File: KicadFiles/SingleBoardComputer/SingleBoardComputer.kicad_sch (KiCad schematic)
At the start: 12 parts

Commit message: Schematic v1.0 done
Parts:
- added C1, C10, C13, C15, C16, C17, C18, C19, C20, C3, C4, C5, C6, C9: 10uF, symbol Device:C
- added C11, C12, C2: 100nF, symbol Device:C
- added C14: 4.7uF, symbol Device:C
- added C7, C8: 47pF, symbol Device:C
- added D1, D2, D3, D4, D5, D6: LED, symbol Device:LED
- added FB1: FerriteBead, symbol Device:FerriteBead
- added L1: 2.2uH, symbol Device:L
- added R1, R10, R11, R2, R5, R6, R7, R8, R9: 5.1k, symbol Device:R
- added R12, R13, R14, R15, R16, R17: 220, symbol Device:R
- added R3, R4: 27, symbol Device:R
- added TP1, TP2, TP3, TP4, TP5, TP6, TP7, TP8, TP? (x2): TestPoint, symbol Connector:TestPoint
- added U3: ISL9110IRT7Z-T7A, Package_DFN_QFN:DFN-12-1EP_3x3mm_P0.5mm_EP1.6x2.5mm_ThermalVias, symbol CustomComponents:ISL9110IRT7Z-T7A
- J1: renamed from J?; symbol Connector:USB_C_Receptacle_USB2.0_16P -> CustomComponents:USB_C_Receptacle_USB2.0_16P_Custom
- SW1: renamed from SW?; footprint (none) -> Button_Switch_SMD:SW_SPST_PTS647_Sx38
- U4, U6: renamed from U?; symbol Memory_Flash:SST39SF040 -> CustomComponents:SST39SF040_Custom
- gave numbers to parts that had none: 8
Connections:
- net USBTP3V3 is gone; now on net UTP_3V3: U5.15 (3V3OUT), U5.3 (VCCIO)
- net +3V3: now also U1.2 (VO), C16.1, C17.1, C18.1, C5.1, D3.2 (A), R10.1, R11.1
- net +5V: now also U1.3 (VI), U4.31 (~{WE}), U6.31 (~{WE}), U8.12 (BGACK), U8.13 (BR), U8.23 (VPA), U8.24 (BERR), C1.1, C10.1, C13.1, C15.1, C19.1, C2.1, C20.1, C3.1, C4.1, D1.2 (A), R5.1, R6.1, R7.1, R8.1, R9.1, U3.1 (VOUT), U3.12 (FB); no longer U5.18 (VCC)
- net A10: now also U2.26 (A9), U4.26 (A9), U6.26 (A9); no longer U2.27 (A8), U4.27 (A8), U6.27 (A8)
- net A11: now also U2.25 (A10), U4.23 (A10), U6.23 (A10); no longer U2.26 (A9), U4.26 (A9), U6.26 (A9)
- net A12: now also U2.24 (A11), U4.25 (A11), U6.25 (A11); no longer U2.25 (A10), U4.23 (A10), U6.23 (A10)
- net A13: now also U2.21 (A12), U4.4 (A12), U6.4 (A12); no longer U2.24 (A11), U4.25 (A11), U6.25 (A11)
- net A14: now also U2.20 (A13), U4.28 (A13), U6.28 (A13); no longer U2.21 (A12), U4.4 (A12), U6.4 (A12)
- net A15: now also U2.19 (A14), U4.29 (A14), U6.29 (A14); no longer U2.20 (A13), U4.28 (A13), U6.28 (A13)
- net A16: now also U2.18 (A15), U4.3 (A15), U6.3 (A15); no longer U2.19 (A14), U4.29 (A14), U6.29 (A14)
- net A17: now also U4.2 (A16), U6.2 (A16); no longer U2.18 (A15), U4.3 (A15), U6.3 (A15)
- net A18: now also U4.30 (A17), U6.30 (A17); no longer U4.2 (A16), U6.2 (A16)
- net A19: now also U4.1 (A18), U6.1 (A18); no longer U4.30 (A17), U6.30 (A17)
- net A2: now also U2.4 (A1), U4.11 (A1), U6.11 (A1); no longer U2.5 (A0), U4.12 (A0), U6.12 (A0)
- net A20: no longer U4.1 (A18), U6.1 (A18)
- net A3: now also U2.3 (A2), U4.10 (A2), U6.10 (A2); no longer U2.4 (A1), U4.11 (A1), U6.11 (A1)
- net A4: now also U2.2 (A3), U4.9 (A3), U6.9 (A3); no longer U2.3 (A2), U4.10 (A2), U6.10 (A2)
- net A5: now also U2.1 (A4), U4.8 (A4), U6.8 (A4); no longer U2.2 (A3), U4.9 (A3), U6.9 (A3)
- net A6: now also U2.44 (A5), U4.7 (A5), U6.7 (A5); no longer U2.1 (A4), U4.8 (A4), U6.8 (A4)
- net A7: now also U2.43 (A6), U4.6 (A6), U6.6 (A6); no longer U2.44 (A5), U4.7 (A5), U6.7 (A5)
- net A8: now also U2.42 (A7), U4.5 (A7), U6.5 (A7); no longer U2.43 (A6), U4.6 (A6), U6.6 (A6)
- net A9: now also U2.27 (A8), U4.27 (A8), U6.27 (A8); no longer U2.42 (A7), U4.5 (A7), U6.5 (A7)
- net CLK: now also U7.7 (I/O/GCK3), D4.2 (A), TP1.1; no longer U7.1 (P1)
- net CPU_LDS: now also U2.39 (~{LB}); no longer U7.19 (P19)
- net CPU_UDS: now also U2.40 (~{UB}); no longer U7.18 (P18)
- net D0: now also U5.24 (DATA0)
- net D1: now also U5.4 (DATA1)
- net D2: now also U5.2 (DATA2)
- net D3: now also U5.9 (DATA3)
- net D4: now also U5.1 (DATA4)
- net D5: now also U5.7 (DATA5)
- net D6: now also U5.8 (DATA6)
- net D7: now also U5.5 (DATA7)
- net GND: now also J1.A1 (GND), J1.A12 (GND), J1.B1 (GND), J1.B12 (GND), SW1.2 (B), U1.1 (GND), C1.2, C10.2, C11.2, C12.2, C13.2, C14.2, C15.2, C16.2, C17.2, C18.2, C19.2, C2.2, C20.2, C3.2, C4.2, C5.2, C6.2, C7.2, C8.2, C9.2, R1.2, R12.2, R13.2, R14.2, R15.2, R16.2, R17.2, R2.1, U3.11 (GND), U3.3 (PGND)
- net RAM_CE: now also U7.25 (P25); no longer U7.27 (P27)
- net ROM_0_CE: now also U7.28 (P28); no longer U7.25 (P25)
- net ROM_1_CE: now also U7.29 (P29); no longer U7.26 (P26)
- net USBD+: now also C7.1, C8.1, R4.2; no longer U5.13 (USBDP)
- net USBD-: now also R3.2; no longer U5.14 (USBDM)
- net UTP_SIWU: now reaches U5.10 (~{SI/WU})
- net UTP_SIWU: now also U7.9 (P9)
- net UTP_RD: now reaches U5.11 (~{RD})
- net UTP_RD: now also U7.36 (P36), TP?.1
- net UTP_WR: now reaches U5.12 (~{WR})
- net UTP_WR: now also U7.35 (P35), TP?.1
- net UTP_3V3: now reaches U5.16 (~{RESET})
- net UTP_3V3: now also C11.1
- net UTP_TXE: now reaches U5.20 (~{TXE})
- net UTP_TXE: now also U7.37 (P37), TP7.1
- net UTP_RXF: now reaches U5.21 (~{RXF})
- net UTP_RXF: now also U7.38 (P38), TP6.1
- net UTP_CBUS6: now reaches U5.22 (CBUS6)
- net UTP_CBUS6: now also U7.43 (P43), TP5.1
- net UTP_CBUS5: now reaches U5.23 (CBUS5)
- net UTP_CBUS5: now also U7.44 (P44), TP8.1
- net RAM_WE: now reaches U2.17 (~{WE})
- net RAM_WE: now also U7.26 (P26)
- net RAM_OE: now reaches U2.41 (~{OE})
- net RAM_OE: now also U7.27 (P27)
- net CPU_DTACK: now reaches U8.10 (DTACK)
- net CPU_DTACK: now also U7.4 (P4), R6.2, TP4.1
- net CPU_HALT: now reaches U8.19 (HALT)
- net CPU_HALT: now also U7.19 (P19), D5.2 (A), R10.2
- net CPU_RST: now reaches U8.20 (RESET)
- net CPU_RST: now also U7.18 (P18), D6.2 (A), R11.2
- net CPU_IPL2: now reaches U8.25 (IPL2)
- net CPU_IPL2: now also U7.3 (P3), R7.2
- net CPU_IPL1: now reaches U8.26 (IPL1)
- net CPU_IPL1: now also U7.2 (P2), R8.2
- net CPU_IPL0: now reaches U8.27 (IPL0)
- net CPU_IPL0: now also U7.1 (P1), R9.2
- net CPU_FC2: now reaches U8.28 (FC2)
- net CPU_FC2: now also U7.22 (P22)
- net CPU_FC1: now reaches U8.29 (FC1)
- net CPU_FC1: now also U7.24 (P24)
- net CPU_FC0: now reaches U8.30 (FC0)
- net CPU_FC0: now also U7.20 (P20)
- net A1: now reaches U8.32 (A1)
- net A1: now also U2.5 (A0), U4.12 (A0), U6.12 (A0)
- net CPU_AS: now reaches U8.6 (AS)
- net CPU_AS: now also U7.5 (I/O/GCK1), TP2.1
- net CPU_R/W: now reaches U8.9 (R/W)
- net CPU_R/W: now also U7.6 (I/O/GCK2), TP3.1
- net ROM_1_OE: now reaches U4.24 (~{OE})
- net ROM_1_OE: now also U7.34 (P34)
- net R_BTN: now reaches SW1.1 (A)
- net R_BTN: now also U7.39 (I/O/GSR), R5.2
- net ROM_0_OE: now reaches U6.24 (~{OE})
- net ROM_0_OE: now also U7.33 (P33)
- net RegBAT: now reaches U7.40 (I/O/GTS2)
- net RegBAT: now also U3.8 (~{BAT})
- net RegPG: now reaches U7.42 (I/O/GTS1)
- net RegPG: now also U3.7 (PG)
- net C_EN: now reaches U7.8 (P8)
- net C_EN: now also Y1.1 (EN)
- net at J1.A4 (VBUS), J1.A9 (VBUS), J1.B4 (VBUS)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: now also C9.1, FB1.1
- net at J1.A5 (CC1): now also R1.1
- net at J1.B5 (CC2): now also R2.2
- new net: D3.1 (K), R14.1
- new net: D4.1 (K), R15.1
- new net: L1.1, U3.2 (LX2)
- new net: L1.2, U3.4 (LX1)
- new net: R4.1, U5.13 (USBDP)
- new net: D5.1 (K), R16.1
- new net: D1.1 (K), R12.1
- new net: R3.1, U5.14 (USBDM)
- new net: D6.1 (K), R17.1
- new net: D2.1 (K), R13.1
- new net +5VD: C12.1, C14.1, C6.1, D2.2 (A), FB1.2, U3.10 (MODE/SYNC), U3.5 (PVIN), U3.6 (VIN), U3.9 (EN), U5.18 (VCC)
- no-connect marks 6 -> 9
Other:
- note added: "0.5MB x 2 ROM Chips"
- note added: "100kB RAM Chip"
- note added: "3V Regulator"
- note added: "5V Regulator"
- note added: "CPLD"
- note added: "Clock"
- note added: "JTAG Header"
- note added: "LEDs"
- note added: "Microprocessor"
- note added: "Power Flags"
- note added: "Pull up to 5V"
- note added: "Request 5V"
- note added: "Reset Button"
- note added: "Test Points"
- note added: "USB to Parallel"
- note added: "USB-C 2.0 Port"
- company: (none) -> Letourneau University
- title: (none) -> Single Board Computer
- moved on the sheet: J1, J2, SW1A, SW1B, U1, U2, U4, U5, U6, U7, U8, Y1

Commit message: Schematic V2.0
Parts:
- removed R10, R11, R6, R7, R8, R9: 5.1k, symbol Device:R
- added R12, R13, R14, R15, R16, R17, R18, R19, R20, R21, R22, R23, R24, R25, R26, R27, R28, R29, R30, R31, R32, R33, R34, R35: 5.1k, symbol Device:R
- gave numbers to parts that had none: 2
- renumbered C12 to C1, C8 to C10, C2 to C11, C5 to C12, C1 to C13, C16 to C14, C17 to C15, C18 to C16, C13 to C17, C15 to C18, C3 to C19, C14 to C2, C4 to C20, C19 to C3, C20 to C4, C6 to C5, C9 to C6, C11 to C7, C10 to C8, C7 to C9, R16 to R10, R17 to R11, R12 to R6, R13 to R7, R14 to R8, R15 to R9, TP2 to TP1, TP1 to TP2, TP6 to TP4, TP4 to TP5, TP7 to TP6, TP5 to TP7, U3 to U1, U5 to U2, U1 to U3, U8 to U4, U7 to U5, U4 to U6, U6 to U7, U2 to U8
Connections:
- net +5V: now also R12.1, R13.1, R14.1, R15.1, R16.1, R17.1, R18.1, R19.1, R20.1, R21.1, R22.1, R23.1, R24.1, R25.1, R26.1, R27.1, R28.1, R29.1, R30.1, R31.1, R32.1, R33.1, R34.1, R35.1
- net CPU_AS: now also R22.2
- net CPU_DTACK: now also R23.2
- net CPU_FC0: now also R29.2
- net CPU_FC1: now also R30.2
- net CPU_FC2: now also R31.2
- net CPU_HALT: now also R28.2
- net CPU_IPL0: now also R26.2
- net CPU_IPL1: now also R25.2
- net CPU_IPL2: now also R24.2
- net CPU_RST: now also R27.2
- net CPU_R/W: now also R21.2
- net C_EN: now also R20.2
- net RAM_CE: now also R12.2
- net RAM_OE: now also R14.2
- net RAM_WE: now also R13.2
- net ROM_0_CE: now also R32.2
- net ROM_0_OE: now also R34.2
- net ROM_1_CE: now also R33.2
- net ROM_1_OE: now also R35.2
- net R_BTN: now also R19.2
- net RegBAT: now also R18.2
- net RegPG: now also R17.2
- net UTP_CBUS5: now also R15.2
- net UTP_CBUS6: now also R16.2
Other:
- note added: "131kB RAM Chip"
- note removed: "100kB RAM Chip"
- moved on the sheet: C1, C10, C11, C12, C13, C14, C15, C16, C17, C18, C19, C2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

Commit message: Changed 5V regulator to TPS63070 (which JLCPCB can provide and solder)
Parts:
- removed C14, C15, C16, C17, C18: 10uF, symbol Device:C
- removed TP1, TP10, TP2, TP3, TP4, TP5, TP6, TP7, TP8, TP9: TestPoint, symbol Connector:TestPoint
- removed U1: ISL9110IRT7Z-T7A, Package_DFN_QFN:DFN-12-1EP_3x3mm_P0.5mm_EP1.6x2.5mm_ThermalVias, symbol CustomComponents:ISL9110IRT7Z-T7A
- added C10, C11, C21, C22, C23, C24, C25, C26: 100nF, Capacitor_SMD:C_0603_1608Metric_Pad1.08x0.95mm_HandSolder, symbol Device:C
- added C6, C9: 10uF, Capacitor_SMD:C_0603_1608Metric_Pad1.08x0.95mm_HandSolder, symbol Device:C
- added C7: 10uF, Capacitor_SMD:C_0805_2012Metric_Pad1.18x1.45mm_HandSolder, symbol Device:C
- added J3: Conn_01x10_Pin, Connector_PinHeader_2.54mm:PinHeader_1x10_P2.54mm_Vertical, symbol Connector:Conn_01x10_Pin
- added R1: 10k, Resistor_SMD:R_0805_2012Metric_Pad1.20x1.40mm_HandSolder, symbol Device:R
- added R7: 100k, Resistor_SMD:R_0805_2012Metric_Pad1.20x1.40mm_HandSolder, symbol Device:R
- added R8: 0, Resistor_SMD:R_0805_2012Metric_Pad1.20x1.40mm_HandSolder, symbol Device:R
- added U1: TPS630701RNMT, RNM0015A, symbol CustomComponents:TPS630701RNMT
- C1, C2: footprint (none) -> Capacitor_SMD:C_0603_1608Metric_Pad1.08x0.95mm_HandSolder
- C12: renamed from C6; footprint (none) -> Capacitor_SMD:C_0805_2012Metric_Pad1.18x1.45mm_HandSolder
- C13: value 10uF -> 100nF; footprint (none) -> Capacitor_SMD:C_0402_1005Metric_Pad0.74x0.62mm_HandSolder
- C14: renamed from C7; footprint (none) -> Capacitor_SMD:C_0603_1608Metric_Pad1.08x0.95mm_HandSolder
- C15: renamed from C9; footprint (none) -> Capacitor_SMD:C_0805_2012Metric_Pad1.18x1.45mm_HandSolder
- C16: renamed from C10; footprint (none) -> Capacitor_SMD:C_0805_2012Metric_Pad1.18x1.45mm_HandSolder
- C17: renamed from C11; footprint (none) -> Capacitor_SMD:C_0603_1608Metric_Pad1.08x0.95mm_HandSolder
- C18: renamed from C12; footprint (none) -> Capacitor_SMD:C_0805_2012Metric_Pad1.18x1.45mm_HandSolder
- C19, C20: value 10uF -> 100nF; footprint (none) -> Capacitor_SMD:C_0603_1608Metric_Pad1.08x0.95mm_HandSolder
- C3, C4, C5: value 10uF -> 22uF; footprint (none) -> Capacitor_SMD:C_0805_2012Metric_Pad1.18x1.45mm_HandSolder
- C8: footprint (none) -> Capacitor_SMD:C_0805_2012Metric_Pad1.18x1.45mm_HandSolder
- D1, D2, D3, D4, D5, D6: footprint (none) -> LED_SMD:LED_0805_2012Metric_Pad1.15x1.40mm_HandSolder
- FB1: footprint (none) -> Inductor_SMD:L_0805_2012Metric_Pad1.15x1.40mm_HandSolder
- J1: footprint (none) -> CustomComponents:CUI_UJ20-C-V-C-3-SMT-TR
- L1: value 2.2uH -> L; footprint (none) -> Inductor_SMD:L_Coilcraft_XxL4020
- R10: renamed from R7; footprint (none) -> Resistor_SMD:R_0805_2012Metric_Pad1.20x1.40mm_HandSolder
- R11: renamed from R8; footprint (none) -> Resistor_SMD:R_0805_2012Metric_Pad1.20x1.40mm_HandSolder
- R12: renamed from R9; footprint (none) -> Resistor_SMD:R_0805_2012Metric_Pad1.20x1.40mm_HandSolder
- R13: renamed from R10; footprint (none) -> Resistor_SMD:R_0805_2012Metric_Pad1.20x1.40mm_HandSolder
- R14: renamed from R11; footprint (none) -> Resistor_SMD:R_0805_2012Metric_Pad1.20x1.40mm_HandSolder
- R15: renamed from R20; footprint (none) -> Resistor_SMD:R_0805_2012Metric_Pad1.20x1.40mm_HandSolder; now fitted
- R16: renamed from R12; footprint (none) -> Resistor_SMD:R_0805_2012Metric_Pad1.20x1.40mm_HandSolder
- R17: renamed from R13; footprint (none) -> Resistor_SMD:R_0805_2012Metric_Pad1.20x1.40mm_HandSolder
- R18: renamed from R14; footprint (none) -> Resistor_SMD:R_0805_2012Metric_Pad1.20x1.40mm_HandSolder
- R19: renamed from R15; footprint (none) -> Resistor_SMD:R_0805_2012Metric_Pad1.20x1.40mm_HandSolder
- R2: renamed from R1; footprint (none) -> Resistor_SMD:R_0805_2012Metric_Pad1.20x1.40mm_HandSolder
- R20: renamed from R16; footprint (none) -> Resistor_SMD:R_0805_2012Metric_Pad1.20x1.40mm_HandSolder
- R21: renamed from R17; footprint (none) -> Resistor_SMD:R_0805_2012Metric_Pad1.20x1.40mm_HandSolder
- R22: renamed from R18; footprint (none) -> Resistor_SMD:R_0805_2012Metric_Pad1.20x1.40mm_HandSolder
- R23: renamed from R19; footprint (none) -> Resistor_SMD:R_0805_2012Metric_Pad1.20x1.40mm_HandSolder
- R24: renamed from R21; footprint (none) -> Resistor_SMD:R_0805_2012Metric_Pad1.20x1.40mm_HandSolder
- R25: renamed from R22; footprint (none) -> Resistor_SMD:R_0805_2012Metric_Pad1.20x1.40mm_HandSolder
- R26: renamed from R23; footprint (none) -> Resistor_SMD:R_0805_2012Metric_Pad1.20x1.40mm_HandSolder
- R27: renamed from R24; footprint (none) -> Resistor_SMD:R_0805_2012Metric_Pad1.20x1.40mm_HandSolder
- R28: renamed from R25; footprint (none) -> Resistor_SMD:R_0805_2012Metric_Pad1.20x1.40mm_HandSolder
- R29: renamed from R26; footprint (none) -> Resistor_SMD:R_0805_2012Metric_Pad1.20x1.40mm_HandSolder
- R3: renamed from R2; footprint (none) -> Resistor_SMD:R_0805_2012Metric_Pad1.20x1.40mm_HandSolder
- R30: renamed from R27; footprint (none) -> Resistor_SMD:R_0805_2012Metric_Pad1.20x1.40mm_HandSolder
- R31: renamed from R28; footprint (none) -> Resistor_SMD:R_0805_2012Metric_Pad1.20x1.40mm_HandSolder
- R32: renamed from R29; footprint (none) -> Resistor_SMD:R_0805_2012Metric_Pad1.20x1.40mm_HandSolder
- R33: renamed from R30; footprint (none) -> Resistor_SMD:R_0805_2012Metric_Pad1.20x1.40mm_HandSolder
- R34: renamed from R31; footprint (none) -> Resistor_SMD:R_0805_2012Metric_Pad1.20x1.40mm_HandSolder
- R35: renamed from R32; footprint (none) -> Resistor_SMD:R_0805_2012Metric_Pad1.20x1.40mm_HandSolder
- R36: renamed from R33; footprint (none) -> Resistor_SMD:R_0805_2012Metric_Pad1.20x1.40mm_HandSolder
- R37: renamed from R34; footprint (none) -> Resistor_SMD:R_0805_2012Metric_Pad1.20x1.40mm_HandSolder
- R38: renamed from R35; footprint (none) -> Resistor_SMD:R_0805_2012Metric_Pad1.20x1.40mm_HandSolder
- R4: renamed from R3; footprint (none) -> Resistor_SMD:R_0805_2012Metric_Pad1.20x1.40mm_HandSolder
- R5: renamed from R4; footprint (none) -> Resistor_SMD:R_0805_2012Metric_Pad1.20x1.40mm_HandSolder
- R6: renamed from R5; footprint (none) -> Resistor_SMD:R_0805_2012Metric_Pad1.20x1.40mm_HandSolder
- R9: renamed from R6; footprint (none) -> Resistor_SMD:R_0805_2012Metric_Pad1.20x1.40mm_HandSolder
- U4: footprint Package_LCC:PLCC-68 -> Package_LCC:PLCC-68_THT-Socket
- U5: footprint CustomComponents:PLCC-44_16.6x16.6mm_P1.27mm -> Package_LCC:PLCC-44_THT-Socket
- U6, U7: value SST39SF040 -> SST39SF040-70-4C-PHE; footprint Package_LCC:PLCC-32_11.4x14.0mm_P1.27mm -> Package_DIP:DIP-32_W15.24mm_Socket_LongPads
- U8: value AS7C1026B-12JCN -> AS7C1026B-12TCN; footprint Package_DIP:DIP-32_W15.24mm -> CustomComponents:TSOP-44_MIL400_ALL-M
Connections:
- net +3V3: now also C20.1, J2.1 (Pin_1), C21.1, C22.1; no longer J2.2 (Pin_2)
- net +5V: now also C3.2, C4.2, C5.2, C10.1, C11.1, C23.1, C24.1, C25.1, C26.1, C9.1, R7.1, U1.5 (FB), U1.8 (VOUT); no longer C13.1, C20.1, C3.1, C4.1, C8.1
- net +5VD: now also C8.1, C6.2, C7.1, R1.1, U1.12 (VIN), U1.13 (VIN); no longer C5.1
- net CLK: now also J3.10 (Pin_10)
- net CPU_AS: now also J3.9 (Pin_9)
- net CPU_DTACK: now also J3.5 (Pin_5)
- net CPU_R/W: now also J3.7 (Pin_7)
- net GND: now also C3.1, C4.1, C5.1, J2.2 (Pin_2), C10.2, C11.2, C21.2, C22.2, C23.2, C24.2, C25.2, C26.2, C6.1, C7.2, C9.2, R8.2, U1.10 (PGND), U1.15 (VSEL), U1.4 (GND), U1.6 (FB2); no longer C3.2, C4.2, C5.2, J2.1 (Pin_1)
- net UTP_CBUS5: now also J3.4 (Pin_4)
- net UTP_CBUS6: now also J3.3 (Pin_3)
- net UTP_RD: now also J3.2 (Pin_2)
- net UTP_RXF: now also J3.8 (Pin_8)
- net UTP_TXE: now also J3.6 (Pin_6)
- net UTP_WR: now also J3.1 (Pin_1)
- net at L1.1: now also U1.11 (L1)
- net at L1.2: now also U1.9 (L2)
- net at J1.S1 (SHIELD): now also R8.1
- new net: R1.2, U1.1 (PS_SYNC), U1.14 (EN)
- new net: R7.2, U1.2 (PG)
- new net: C13.1, U1.3 (VAUX)
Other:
- moved on the sheet: D1, D2, D3, D4, D5, D6, R10, R11, R12, R13, R14, R9

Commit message: Updated some schematic, added sockets to BOM, building PCB
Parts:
- removed R23: 5.1k, Resistor_SMD:R_0805_2012Metric_Pad1.20x1.40mm_HandSolder, symbol Device:R
- removed unit 2 of SW1
- added U?: 8444-11B1-RK-TP, TO_11B1-RK-TP_3MM, symbol CustomComponents:8444-11B1-RK-TP
- added U?: 8468-11B1-RK-TP, Package_LCC:PLCC-68_THT-Socket, symbol CustomComponents:8468-11B1-RK-TP
- R10, R11, R12, R13, R14, R9: value 220 -> 1k
- R19, R20, R21, R22: now left out of the parts list
- R23: renamed from R24; now left out of the parts list
- R24: renamed from R25; now left out of the parts list
- R25: renamed from R26; now left out of the parts list
- R26: renamed from R27; now left out of the parts list
- R27: renamed from R28; now left out of the parts list
- R28: renamed from R29; now left out of the parts list
- R29: renamed from R30; now left out of the parts list
- R30: renamed from R31; now left out of the parts list
- R31: renamed from R32; now left out of the parts list
- R32: renamed from R33; now left out of the parts list
- R33: renamed from R34; now left out of the parts list
- R34: renamed from R35; now left out of the parts list
- R35: renamed from R36; now left out of the parts list
- R36: renamed from R37; now left out of the parts list
- R37: renamed from R38; now left out of the parts list
- U8: value AS7C1026B-12TCN -> AS7C1026B-12JCN; footprint CustomComponents:TSOP-44_MIL400_ALL-M -> Package_SO:SOJ-44_10.16x28.575mm_P1.27mm
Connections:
- net +5V: now also U1.7 (VOUT)
- net USBD+: no longer C15.1
- net USBD-: now also C15.1
- no-connect marks 9 -> 6
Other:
- note added: "CPLD Socket"
- note added: "MCU Socket"
- moved on the sheet: C10, C11, C12, C20, C21, C22, R15, R16, R17, R18, R19, R20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

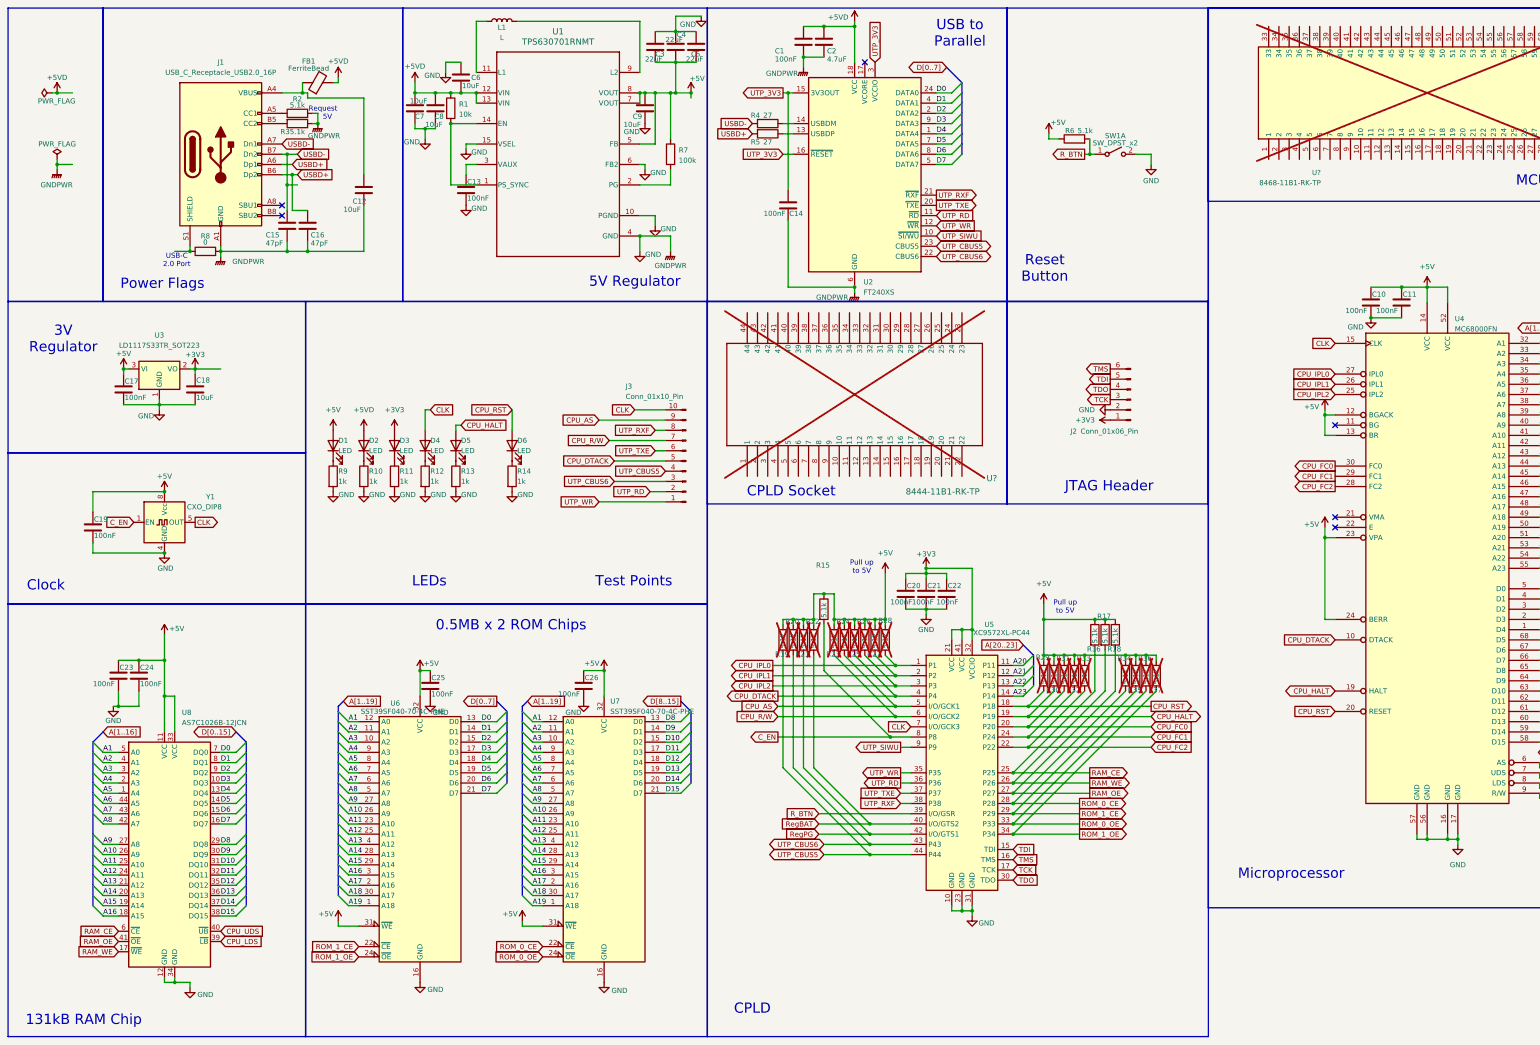
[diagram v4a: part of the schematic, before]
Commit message: PCB before schematic modification
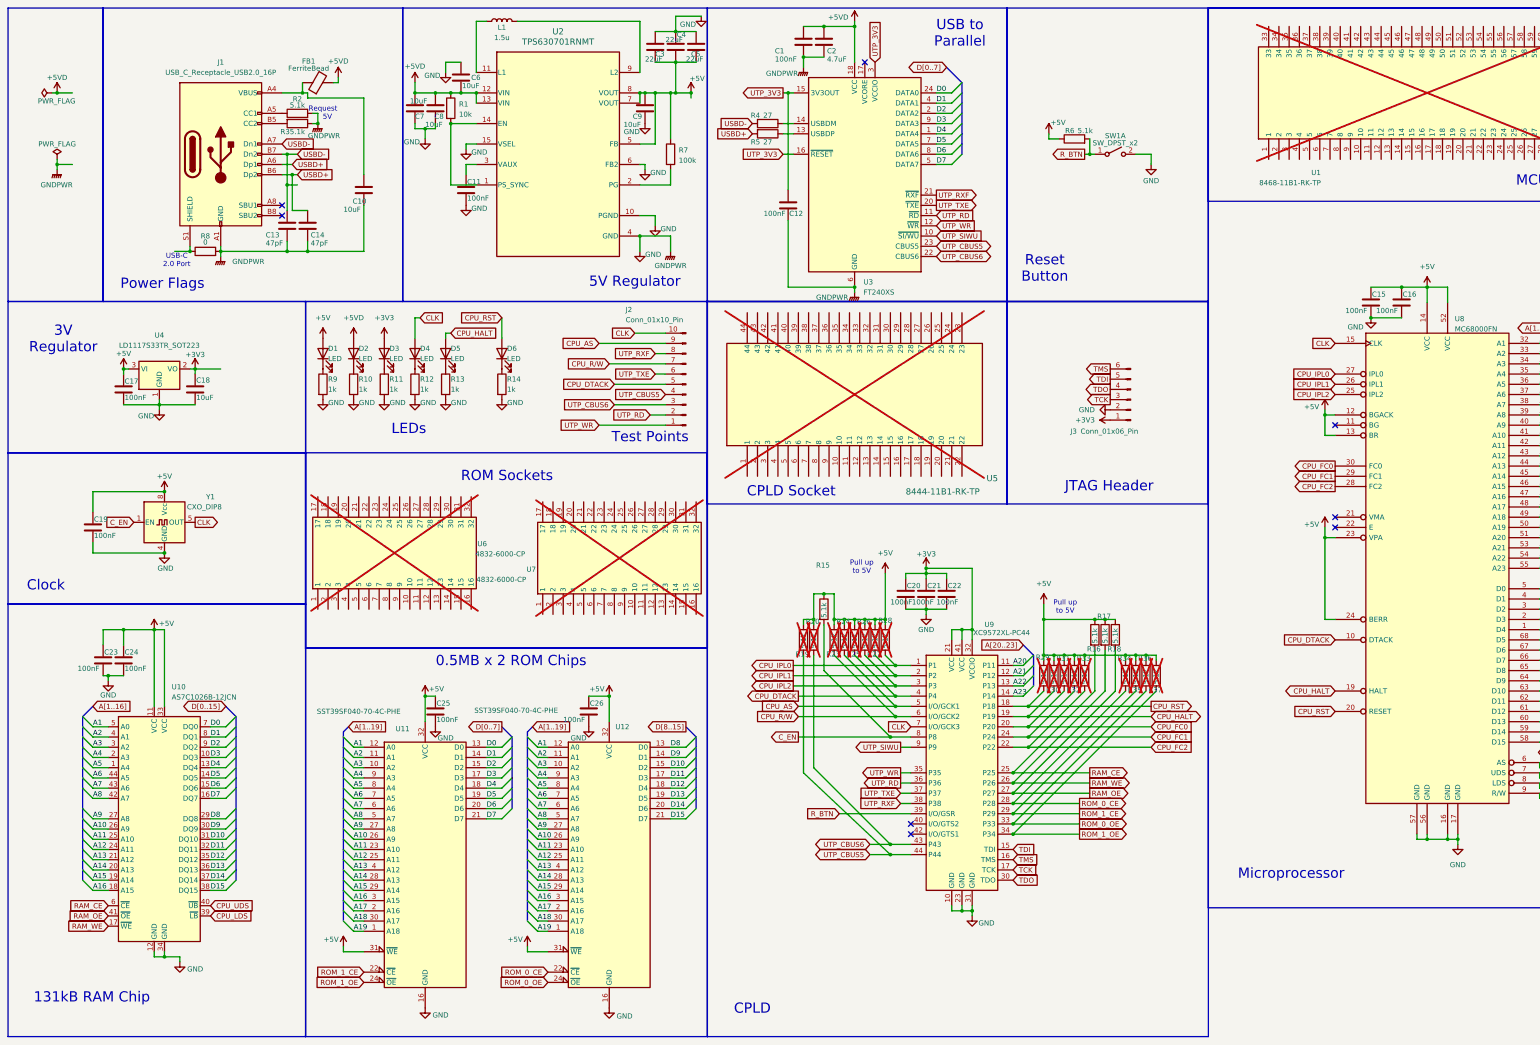
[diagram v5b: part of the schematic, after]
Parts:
- removed R21, R22: 5.1k, Resistor_SMD:R_0805_2012Metric_Pad1.20x1.40mm_HandSolder, symbol Device:R
- added U6, U7: 4832-6000-CP, Package_DIP:DIP-32_W15.24mm_Socket, symbol CustomComponents:DIP-32_Socket_THT
- L1: value L -> 1.5u
- U5: renamed from U?; footprint TO_11B1-RK-TP_3MM -> Package_LCC:PLCC-44_THT-Socket
- gave numbers to parts that had none: 1
- renumbered C12 to C10, C13 to C11, C14 to C12, C15 to C13, C16 to C14, C10 to C15, C11 to C16, J3 to J2, J2 to J3, U8 to U10, U6 to U11, U7 to U12, U1 to U2, U2 to U3, U3 to U4, U4 to U8, U5 to U9
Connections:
- net RegBAT: no longer names the net of U9.40 (I/O/GTS2)
- net RegPG: no longer names the net of U9.42 (I/O/GTS1)
- no-connect marks 6 -> 8
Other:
- note added: "ROM Sockets"
- moved on the sheet: C23, C24, C25, C26, D1, D2, D3, D4, D5, D6, J2, R10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
